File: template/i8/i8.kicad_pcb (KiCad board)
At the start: 2 copper layers, 100 x 100 mm, 43 parts, among them J1 ZX-SH1.0-4PWT, J2 Conn_DEBUG, SW1 MX_SW, SW2 MX_SW, SW3 MX_SW, SW4 MX_SW, U1 RP2040, U2 XC6206P332MR-G, U3 W25Q128JVS, Y1 Crystal_GND24

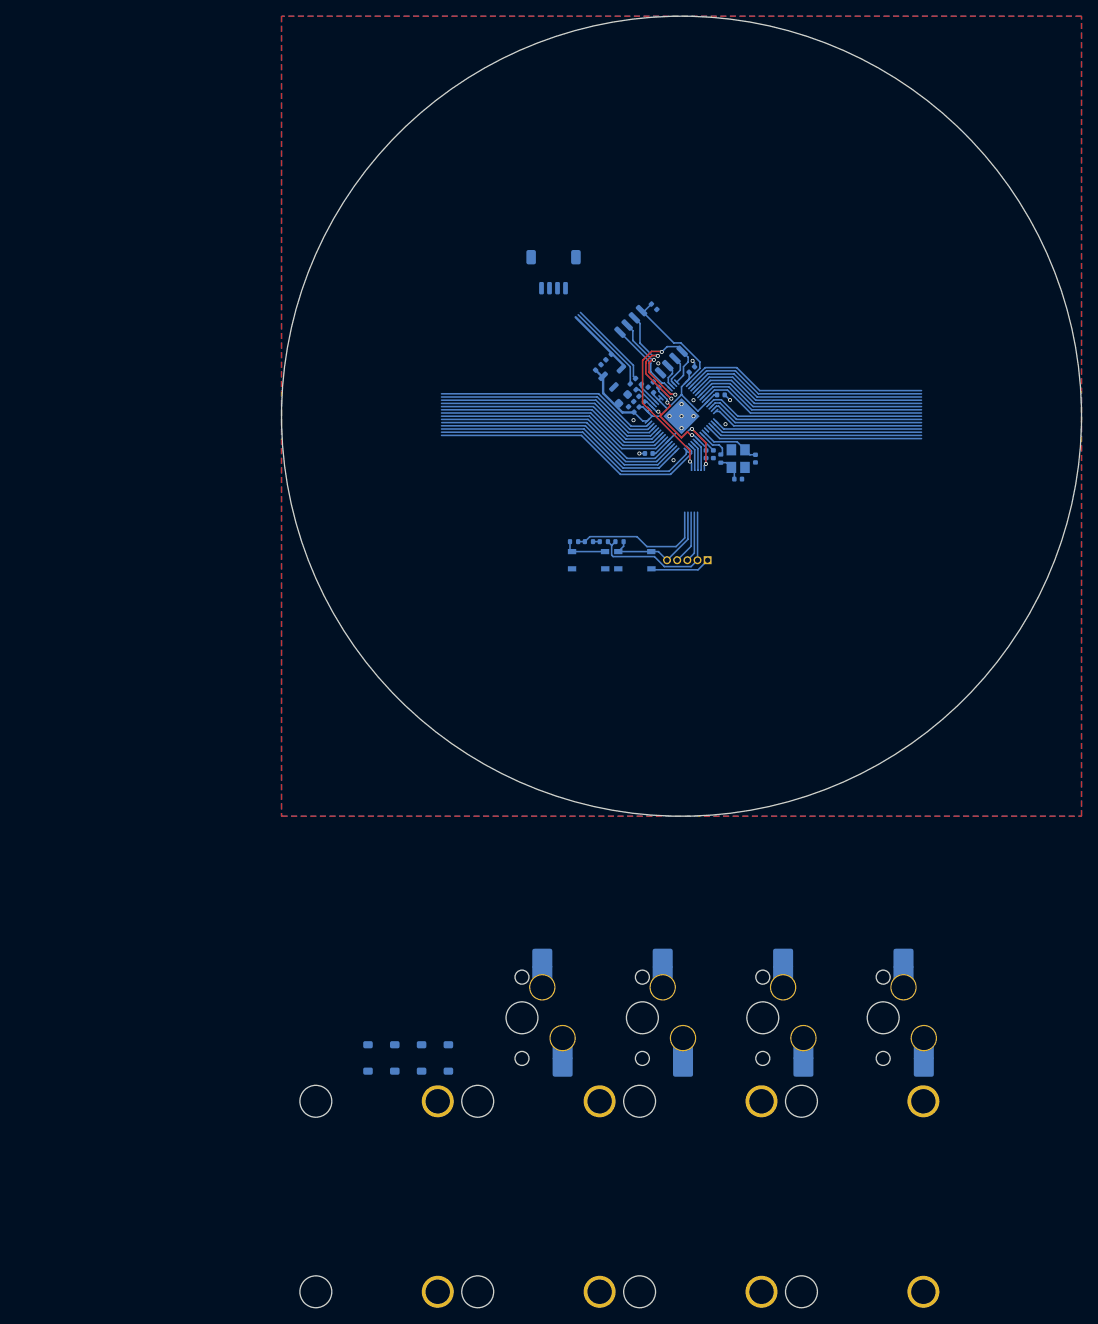
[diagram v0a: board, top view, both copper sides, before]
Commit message: downgraded flash chip
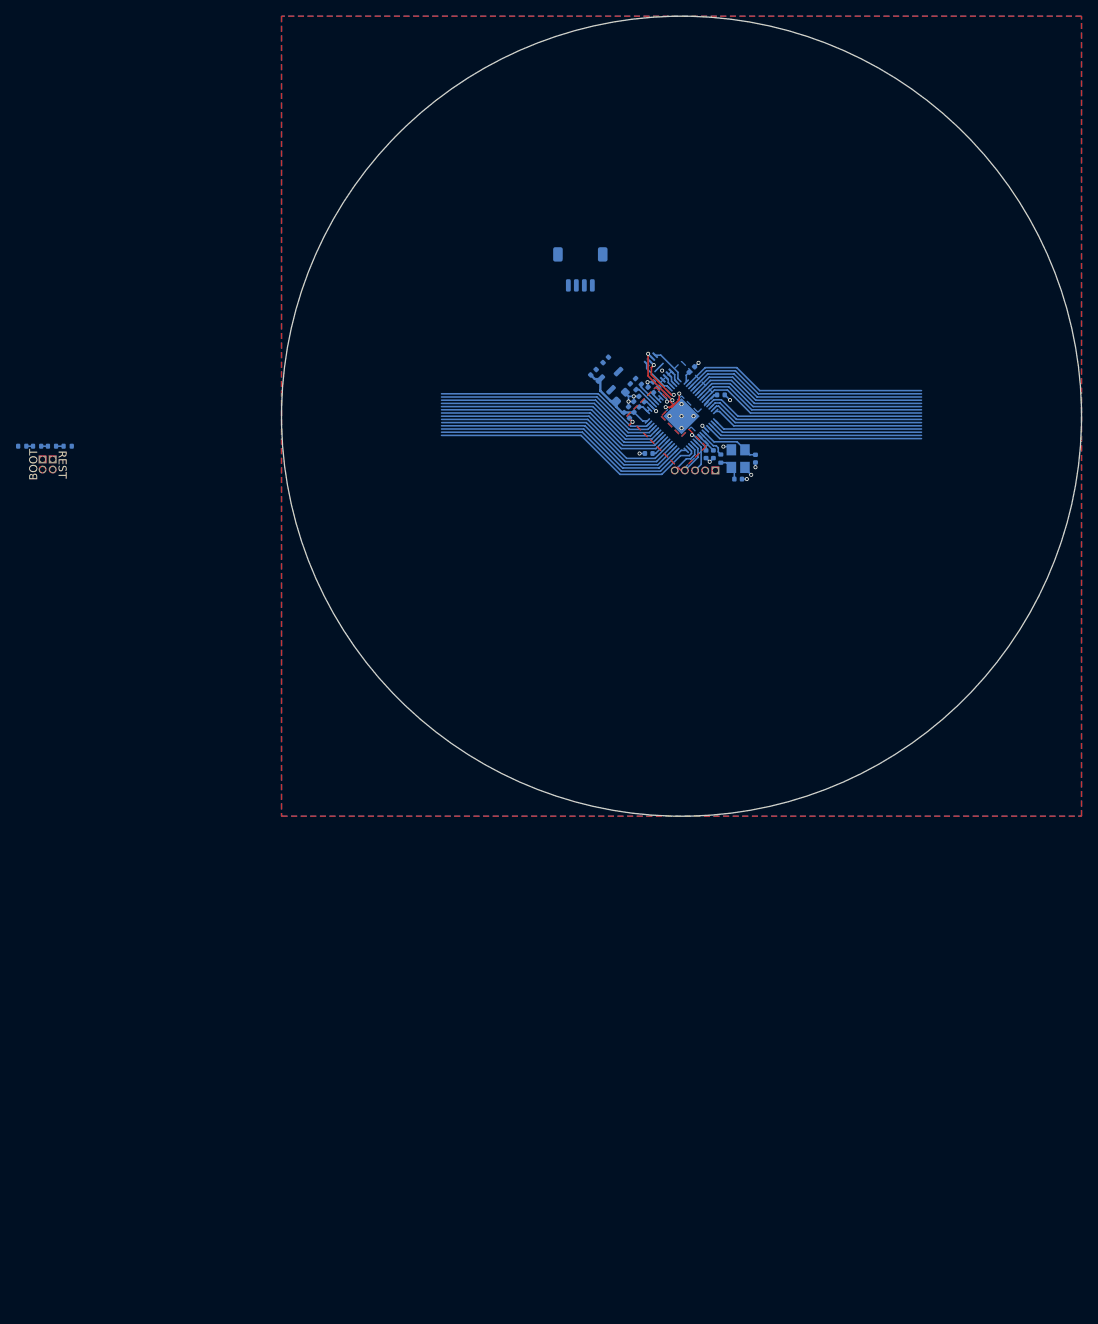
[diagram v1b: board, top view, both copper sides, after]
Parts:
- removed C15: 22p, Capacitor_SMD:C_0402_1005Metric
- removed D1, D2, D3, D4: D, Diode_SMD:D_SOD-123
- removed S1, S2, S3, S4: MX_S, PCM_marbastlib-mx:STAB_MX_P_2u
- removed SW1, SW2, SW3, SW4: MX_SW, PCM_marbastlib-mx:SW_MX_HS_S_CPG151101S11_1u
- added C17: 22p, Capacitor_SMD:C_0402_1005Metric, B.Cu at (7.08, 7.86)
- C12: value 1u -> 100n
- J2: moved to F.Cu
- PSW1: value SKRPACE010 -> REST; footprint Button_Switch_SMD:SW_Push_1P1T_NO_Vertical_Wuerth_434133025816 -> Connector_PinHeader_1.27mm:PinHeader_1x02_P1.27mm_Vertical; moved to F.Cu
- PSW2: value SKRPACE010 -> BOOT; footprint Button_Switch_SMD:SW_Push_1P1T_NO_Vertical_Wuerth_434133025816 -> Connector_PinHeader_1.27mm:PinHeader_1x02_P1.27mm_Vertical; moved to F.Cu
- U1: value RP2040 -> XC6206P332MR-G; footprint Package_DFN_QFN:QFN-56-1EP_7x7mm_P0.4mm_EP3.2x3.2mm -> Package_TO_SOT_SMD:SOT-23-3
- U2: value XC6206P332MR-G -> RP2040; footprint Package_TO_SOT_SMD:SOT-23-3 -> Package_DFN_QFN:QFN-56-1EP_7x7mm_P0.4mm_EP3.2x3.2mm
- U3: value W25Q128JVS -> W25Q16JVUXIQ; footprint Package_SO:SOIC-8_5.3x5.3mm_P1.27mm -> Package_SON:Winbond_USON-8-1EP_3x2mm_P0.5mm_EP0.2x1.6mm
- moved PSW1 73.9 mm to (-78.6, 5.40)
- moved R5 70.0 mm to (-78.7, 3.75)
- moved R3 70.0 mm to (-76.7, 3.75)
- moved R6 70.0 mm to (-80.5, 3.75)
- moved R7 70.0 mm to (-82.4, 3.75)
- moved PSW2 69.4 mm to (-79.9, 5.40)
- moved J2 11.3 mm to (4.23, 6.78), turned to -90 degrees
- moved C14 11.2 mm to (-11.0, -5.49), turned to 45 degrees
- moved U1 9.90 mm to (-8.68, -4.77), turned to 45 degrees
- moved U2 9.77 mm to (-0.00, -0.00), turned to -135 degrees
- moved C12 7.63 mm to (-6.85, -0.10), turned to -45 degrees
- moved U3 3.37 mm to (-2.81, -6.09)
- moved J1 3.37 mm to (-12.7, -18.4)
- moved C16 3.35 mm to (9.24, 5.30), turned to 90 degrees
- moved C13 1.32 mm to (-9.47, -7.04), turned to -135 degrees
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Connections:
- C12 pad 1: +5V -> +3V3
- C13 pad 1: +3V3 -> +5V
- C14 pad 1: GND -> +3V3
- C14 pad 2: +3V3 -> GND
- C16 pad 2: Net-(C16-Pad2) -> XIN
- R1 pad 2: Net-(U1-USB_DP) -> Net-(U2-USB_DP)
- R2 pad 1: Net-(U1-USB_DM) -> Net-(U2-USB_DM)
- R4 pad 2: Net-(C16-Pad2) -> Net-(C17-Pad2)
- U1 pad 1: +3V3 -> GND
- U1 pad 2: GPIO0 -> +3V3
- U1 pad 3: GPIO1 -> +5V
- U2 pad 1: GND -> +3V3
- U2 pad 2: +3V3 -> GPIO0
- U2 pad 3: +5V -> GPIO1
- Y1 pad 1: Net-(C16-Pad2) -> Net-(C17-Pad2)
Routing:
- net +3V3: track 85.5 -> 32.1 mm
- net Q_SEL: track 44.7 -> 2.43 mm, vias 2 -> 0
- net RST: track 18.4 -> 4.63 mm
- net D-: track 11.3 -> 0.00 mm
- net D+: track 11.1 -> 0.00 mm
- net +1V1: track 15.9 -> 6.95 mm
- net +5V: track 8.60 -> 0.00 mm
- net Q_CLK: track 13.5 -> 6.87 mm
- net SWD: track 10.3 -> 4.29 mm
- net SWC: track 10.3 -> 4.26 mm
- net Q_IO3: track 15.2 -> 9.23 mm
- net Net-(PSW2-Pad2): track 5.47 -> 0.00 mm
- net Q_IO0: track 9.83 -> 4.56 mm
- net GND: track 10.2 -> 15.4 mm, vias 13 -> 19
- net Net-(C17-Pad2): track 0.00 -> 3.18 mm
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- added copper zone on F.Cu, net +1V1
- added copper zone on B.Cu, net +3V3
